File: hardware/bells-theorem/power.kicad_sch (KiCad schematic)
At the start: 10 parts, among them J1 Conn_02x05_Odd_Even, U2 R-78B5.0-2.0

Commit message: All changes up to date with latest revisions
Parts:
- added C3: 1uF, Capacitor_THT:CP_Radial_D5.0mm_P2.50mm, symbol Device:C_Polarized_US
- added U3: ADP150-3.3, Package_TO_SOT_SMD:TSOT-23-5, symbol Regulator_Linear:ADP7142AUJZ-3.3
- C1: footprint Capacitor_SMD:C_0805_2012Metric_Pad1.15x1.40mm_HandSolder -> Capacitor_SMD:C_0805_2012Metric_Pad1.18x1.45mm_HandSolder
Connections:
- net +5V: now also U3.1 (VIN)
- net GND: now also C3.2, U3.2 (GND)
- new net +3V3: C3.1, U3.5 (VOUT)
- new net 3Venable: U3.3 (EN)
- no-connect marks 0 -> 1
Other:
- title: (none) -> Bell's Theorem
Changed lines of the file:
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@@
 (kicad_sch (version 20211123) (generator eeschema)
   (paper "A4")
+  (title_block
+    (title "Bell's Theorem")
+    (date "2022-01-16")
+  )
   (junction (at 113.03 73.66) (diameter 0) (color 0 0 0 0)
   )
@@
   (junction (at 76.2 82.55) (diameter 0) (color 0 0 0 0)
   )
+  (junction (at 136.525 113.03) (diameter 0) (color 0 0 0 0)
+  )
   (junction (at 77.47 113.03) (diameter 0) (color 0 0 0 0)
   )
@@
   (junction (at 88.9 73.66) (diameter 0) (color 0 0 0 0)
   )
+  (no_connect (at 130.175 115.57))
   (wire (pts (xy 81.28 113.03) (xy 77.47 113.03))
     (stroke (width 0) (type default) (color 0 0 0 0))
@@
     (stroke (width 0) (type default) (color 0 0 0 0))
   )
+  (wire (pts (xy 136.525 113.03) (xy 136.525 114.935))
+    (stroke (width 0) (type default) (color 0 0 0 0))
+  )
   (wire (pts (xy 96.52 113.03) (xy 99.06 113.03))
     (stroke (width 0) (type default) (color 0 0 0 0))
@@
     (stroke (width 0) (type default) (color 0 0 0 0))
   )
+  (wire (pts (xy 136.525 109.855) (xy 136.525 113.03))
+    (stroke (width 0) (type default) (color 0 0 0 0))
+  )
+  (wire (pts (xy 130.175 113.03) (xy 136.525 113.03))
+    (stroke (width 0) (type default) (color 0 0 0 0))
+  )
   (wire (pts (xy 88.9 91.44) (xy 91.44 91.44))
     (stroke (width 0) (type default) (color 0 0 0 0))
@@
     (stroke (width 0) (type default) (color 0 0 0 0))
   )
+  (wire (pts (xy 107.315 118.11) (xy 107.315 127))
+    (stroke (width 0) (type default) (color 0 0 0 0))
+  )
   (wire (pts (xy 99.06 113.03) (xy 99.06 115.57))
     (stroke (width 0) (type default) (color 0 0 0 0))
@@
     (stroke (width 0) (type default) (color 0 0 0 0))
   )
+  (wire (pts (xy 99.06 113.03) (xy 109.855 113.03))
+    (stroke (width 0) (type default) (color 0 0 0 0))
+  )
   (wire (pts (xy 88.9 73.66) (xy 91.44 73.66))
     (stroke (width 0) (type default) (color 0 0 0 0))
@@
   (wire (pts (xy 113.03 82.55) (xy 120.65 82.55))
     (stroke (width 0) (type default) (color 0 0 0 0))
+  )
+  (wire (pts (xy 109.855 118.11) (xy 107.315 118.11))
+    (stroke (width 0) (type default) (color 0 0 0 0))
+  )
+  (hierarchical_label "3Venable" (shape input) (at 107.315 127 270)
+    (effects (font (size 1.27 1.27)) (justify right))
   )
   (symbol (lib_id "Device:C_Polarized_US") (at 113.03 78.74 0) (unit 1)
@@
       (effects (font (size 1.27 1.27)) (justify left))
     )
-    (property "Footprint" "Capacitor_SMD:C_0805_2012Metric_Pad1.15x1.40mm_HandSolder" (id 2) (at 77.47 118.11 0)
+    (property "Footprint" "Capacitor_SMD:C_0805_2012Metric_Pad1.18x1.45mm_HandSolder" (id 2) (at 77.47 118.11 0)
       (effects (font (size 1.27 1.27)) hide)
     )
@@
       (effects (font (size 1.27 1.27)) hide)
     )
+    (pin "1")
+  )
+  (symbol (lib_id "Regulator_Linear:ADP7142AUJZ-3.3") (at 120.015 115.57 0) (unit 1)
+    (in_bom yes) (on_board yes) (fields_autoplaced)
+    (property "Reference" "U3" (id 0) (at 120.015 106.5235 0))
+    (property "Value" "ADP150-3.3" (id 1) (at 120.015 109.2986 0))
+    (property "Footprint" "Package_TO_SOT_SMD:TSOT-23-5" (id 2) (at 120.015 125.73 0)
+      (effects (font (size 1.27 1.27) italic) hide)
+    )
+    (property "Datasheet" "https://www.analog.com/media/en/technical-documentation/data-sheets/ADP7142.pdf" (id 3) (at 120.015 128.27 0)
+      (effects (font (size 1.27 1.27)) hide)
+    )
+    (pin "1")
+    (pin "2")
+    (pin "3")
+    (pin "4")
+    (pin "5")
+  )
+  (symbol (lib_id "power:+3.3V") (at 136.525 109.855 0) (unit 1)
+    (in_bom yes) (on_board yes) (fields_autoplaced)
+    (property "Reference" "#PWR052" (id 0) (at 136.525 113.665 0)
+      (effects (font (size 1.27 1.27)) hide)
+    )
+    (property "Value" "+3.3V" (id 1) (at 136.525 106.2505 0))
+    (property "Footprint" "" (id 2) (at 136.525 109.855 0)
+      (effects (font (size 1.27 1.27)) hide)
+    )
+    (property "Datasheet" "" (id 3) (at 136.525 109.855 0)
+      (effects (font (size 1.27 1.27)) hide)
+    )
+    (pin "1")
+  )
+  (symbol (lib_id "Device:C_Polarized_US") (at 136.525 118.745 0) (unit 1)
+    (in_bom yes) (on_board yes)
+    (property "Reference" "C3" (id 0) (at 137.16 116.205 0)
+      (effects (font (size 1.27 1.27)) (justify left))
+    )
+    (property "Value" "1uF" (id 1) (at 137.16 121.285 0)
+      (effects (font (size 1.27 1.27)) (justify left))
+    )
+    (property "Footprint" "Capacitor_THT:CP_Radial_D5.0mm_P2.50mm" (id 2) (at 136.525 118.745 0)
+      (effects (font (size 1.27 1.27)) hide)
+    )
+    (property "Datasheet" "~" (id 3) (at 136.525 118.745 0)
+      (effects (font (size 1.27 1.27)) hide)
+    )
+    (pin "1")
+    (pin "2")
+  )
+  (symbol (lib_id "power:GND") (at 136.525 122.555 0) (unit 1)
+    (in_bom yes) (on_board yes)
+    (property "Reference" "#PWR056" (id 0) (at 136.525 128.905 0)
+      (effects (font (size 1.27 1.27)) hide)
+    )
+    (property "Value" "GND" (id 1) (at 136.525 126.365 0))
+    (property "Footprint" "" (id 2) (at 136.525 122.555 0))
+    (property "Datasheet" "" (id 3) (at 136.525 122.555 0))
     (pin "1")
   )
@@
     (pin "3")
   )
+  (symbol (lib_id "power:GND") (at 120.015 123.19 0) (unit 1)
+    (in_bom yes) (on_board yes)
+    (property "Reference" "#PWR051" (id 0) (at 120.015 129.54 0)
+      (effects (font (size 1.27 1.27)) hide)
+    )
+    (property "Value" "GND" (id 1) (at 120.015 127 0))
+    (property "Footprint" "" (id 2) (at 120.015 123.19 0))
+    (property "Datasheet" "" (id 3) (at 120.015 123.19 0))
+    (pin "1")
+  )
 )

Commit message: last hardware / software updates
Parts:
- removed C5: 10uF, Capacitor_THT:CP_Radial_D5.0mm_P2.50mm, symbol Device:C_Polarized_US
- removed D2: CDBM140-G, Diode_SMD:D_SMA-SMB_Universal_Handsoldering, symbol Device:D_Schottky
- removed J1: Conn_02x05_Odd_Even, Connector_IDC:IDC-Header_2x05_P2.54mm_Vertical, symbol Connector_Generic:Conn_02x05_Odd_Even
- removed L2: BLM21PG220SH1D, Inductor_SMD:L_0805_2012Metric_Pad1.15x1.40mm_HandSolder, symbol Device:FerriteBead_Small
- added C61: 10uF, Capacitor_THT:CP_Radial_D5.0mm_P2.50mm, symbol Device:C_Polarized_US
- added J1: Euro_Power, Connector_IDC:IDC-Header_2x08_P2.54mm_Vertical, symbol Connector_Generic:Conn_02x08_Odd_Even
- added J24: 5V_SEL, Connector_PinHeader_2.54mm:PinHeader_1x03_P2.54mm_Vertical, symbol Connector_Generic:Conn_01x03
- added U18: L78L10, Package_TO_SOT_THT:TO-92_Inline_Wide, symbol Regulator_Linear:L78L10_TO92
- C2: value 1uF -> 1uF/10uF
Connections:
- net +12V: now also U18.3 (VI)
- net +5V: now also J24.2 (Pin_2); no longer U2.3 (OUT)
- net GND: now also C61.2, J1.3 (Pin_3), J1.4 (Pin_4), J1.5 (Pin_5), J1.6 (Pin_6), J1.7 (Pin_7), J1.8 (Pin_8), U18.2 (GND)
- net at L1.2: now also J1.10 (Pin_10), J1.9 (Pin_9)
- new net: J1.1 (Pin_1), J1.2 (Pin_2)
- new net: J1.11 (Pin_11), J1.12 (Pin_12), J24.3 (Pin_3)
- new net: J24.1 (Pin_1), U2.3 (OUT)
- new net +10V: C61.1, U18.1 (VO)
- no-connect marks 1 -> 5
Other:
- note added: "Do not need - rails"
- note added: "maybe use LM137 instead"
- moved on the sheet: C1, C2, C3, C4, D1, L1, U2, U3

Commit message: version 0.6 hardware and code
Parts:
- added C19: 10uF, Capacitor_THT:CP_Radial_D5.0mm_P2.50mm, symbol Device:C_Polarized_US
- added C69: 100nF, Capacitor_SMD:C_0805_2012Metric_Pad1.18x1.45mm_HandSolder, symbol Device:C_Small
- added D2: CDBM140-G, Diode_SMD:D_SMA-SMB_Universal_Handsoldering, symbol Device:D_Schottky
- added L2: BLM21PG220SH1D, Inductor_SMD:L_0805_2012Metric_Pad1.15x1.40mm_HandSolder, symbol Device:FerriteBead_Small
- added R101, R102: 10k, Resistor_SMD:R_0805_2012Metric_Pad1.20x1.40mm_HandSolder, symbol Device:R_US
- added U19: TL071, Package_SO:SOIC-8_3.9x4.9mm_P1.27mm, symbol Amplifier_Operational:TL071
- U2: value R-78B5.0-2.0 -> R-785.0-1.0; footprint Converter_DCDC:Converter_DCDC_RECOM_R-78B-2.0_THT -> Converter_DCDC:Converter_DCDC_RECOM_R-78E-0.5_THT
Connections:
- net +10V: now also R101.1
- net +12V: now also U19.7 (V+)
- net GND: now also C19.1, C69.2, U19.3 (+)
- net at J1.1 (Pin_1), J1.2 (Pin_2): now also L2.2
- new net: D2.1 (K), L2.1
- new net: C19.2, C69.1, D2.2 (A), U19.4 (V-)
- new net: R101.2, R102.1, U19.2 (-)
- new net -10V: R102.2, U19.6
- no-connect marks 5 -> 7
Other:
- note removed: "Do not need - rails"

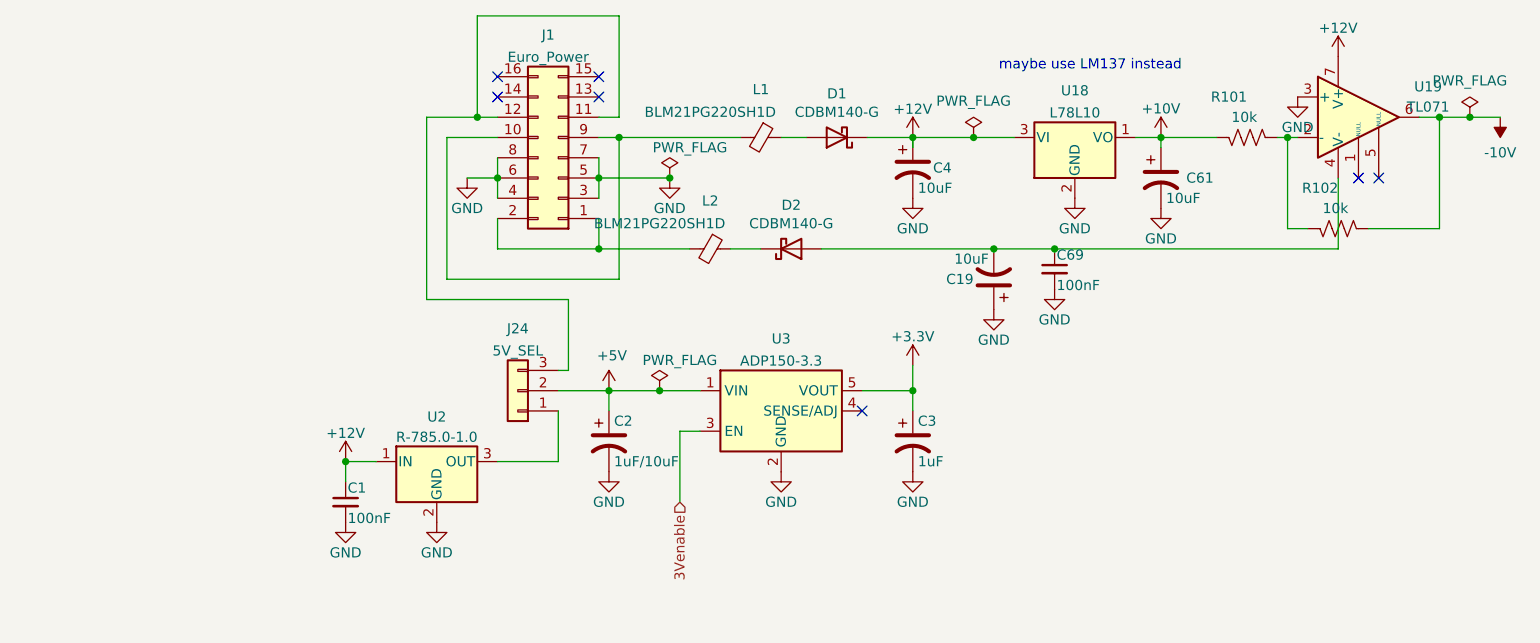
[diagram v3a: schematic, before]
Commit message: current revision actually 0.6 was 1.0 candidate, but needs major revision
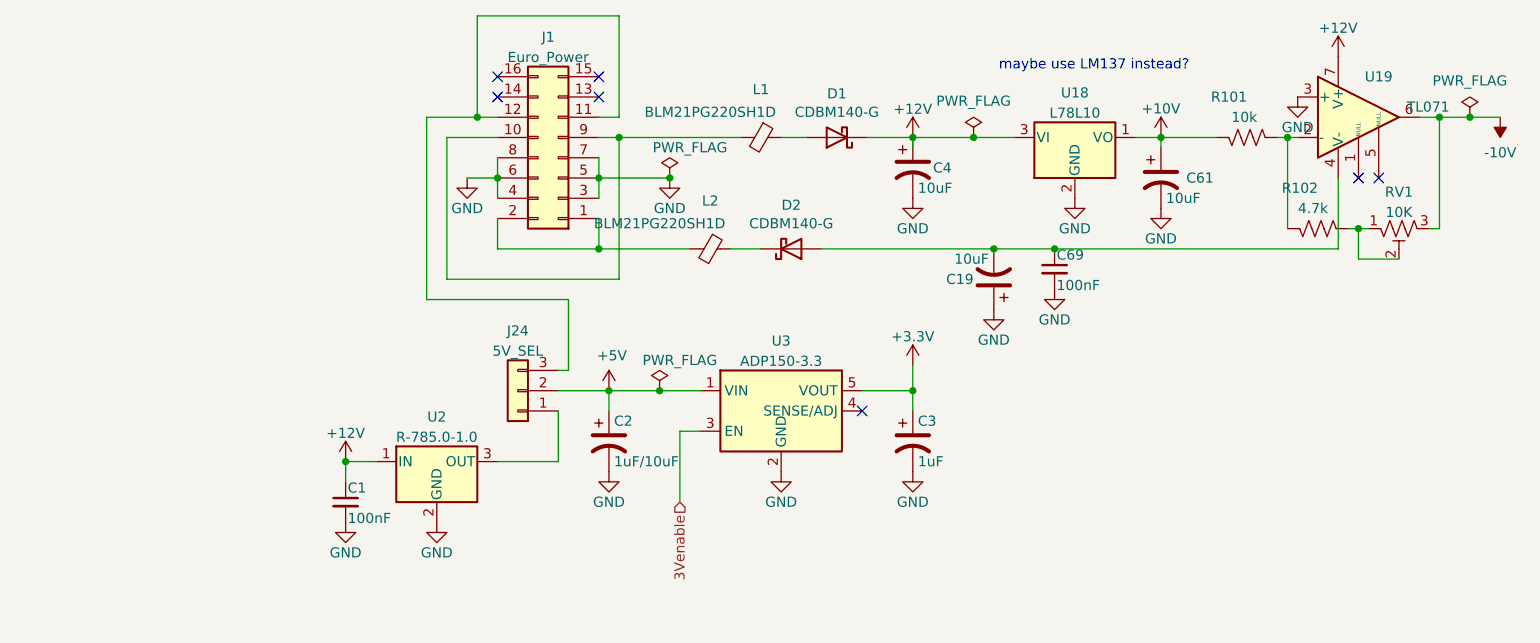
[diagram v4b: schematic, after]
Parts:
- added RV1: 10K, myfootprints:pot_bourns_3296_dual-vertical, symbol Device:R_Potentiometer_Trim_US
- R102: value 10k -> 4.7k
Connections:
- net -10V: now also RV1.3; no longer R102.2
- new net: R102.2, RV1.1, RV1.2
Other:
- note added: "maybe use LM137 instead?"
- note removed: "maybe use LM137 instead"
- moved on the sheet: R102

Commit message: checking in old outstanding changes prior to debugging with Claude Code
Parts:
- removed C61: 10uF, Capacitor_THT:CP_Radial_D5.0mm_P2.50mm, symbol Device:C_Polarized_US
- removed R101: 10k, Resistor_SMD:R_0805_2012Metric_Pad1.20x1.40mm_HandSolder, symbol Device:R_US
- removed R102: 4.7k, Resistor_SMD:R_0805_2012Metric_Pad1.20x1.40mm_HandSolder, symbol Device:R_US
- removed RV1: 10K, myfootprints:pot_bourns_3296_dual-vertical, symbol Device:R_Potentiometer_Trim_US
- removed U18: L78L10, Package_TO_SOT_THT:TO-92_Inline_Wide, symbol Regulator_Linear:L78L10_TO92
- removed U19: TL071, Package_SO:SOIC-8_3.9x4.9mm_P1.27mm, symbol Amplifier_Operational:TL071
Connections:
- net -12V: now reaches C19.2, C69.1, D2.2 (A)
- no-connect marks 7 -> 5
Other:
- note removed: "maybe use LM137 instead?"
- moved on the sheet: C19
